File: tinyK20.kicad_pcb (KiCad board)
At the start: 2 copper layers, 46 x 74.4 mm, 79 parts, among them CON1 USB-MINI-B, P1 CONN_1, P10 CONN_1, P11 CONN_1, P12 CONN_1, P13 CONN_1, P14 CONN_1, P15 CONN_1, P16 CONN_1, P17 CONN_1, P18 CONN_1, P19 CONN_1, P2 CONN_1, P20 CONN_1, P21 CONN_1, P22 CONN_1, P23 CONN_1, P24 CONN_1, P25 CONN_1, P26 CONN_1, P27 CONN_1, P28 CONN_1, P29 CONN_1, P3 CONN_1, P30 CONN_1, P31 CONN_1, P33 CONN_1, P34 CONN_1, P35 CONN_5X2, P37 CONN_1, P38 CONN_5X2, P4 CONN_1, P41 CONN_1, P5 CONN_1, P6 CONN_1, P7 CONN_1, P8 CONN_1, P9 CONN_1, SW1 SW_PUSH, U1 MK20DX128VFT5, U2 LT1129CST-3.3, U3 74LS126, U4 105027-0001, Y1 Crystal, Y2 Crystal_Small

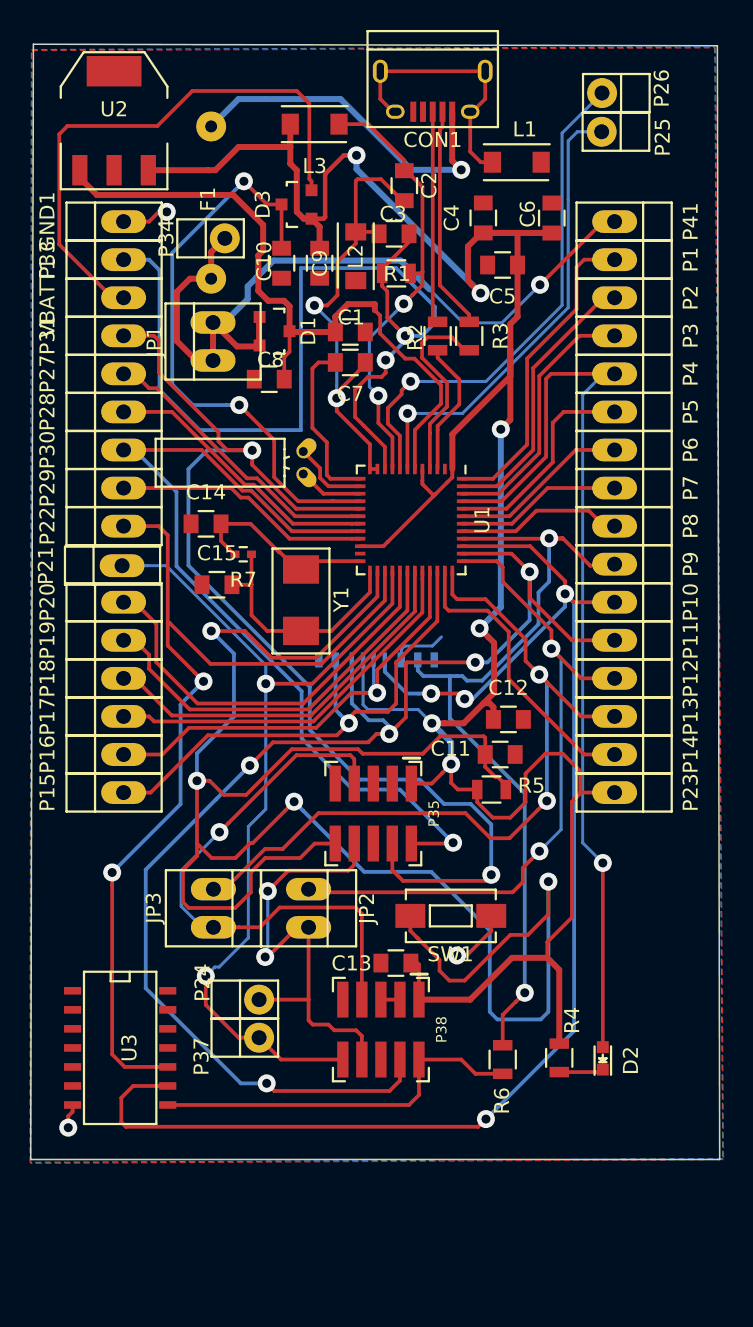
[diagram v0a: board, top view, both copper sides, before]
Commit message: Get rid of ground plane on top copper.
 Add optional vias. Re-route tracks
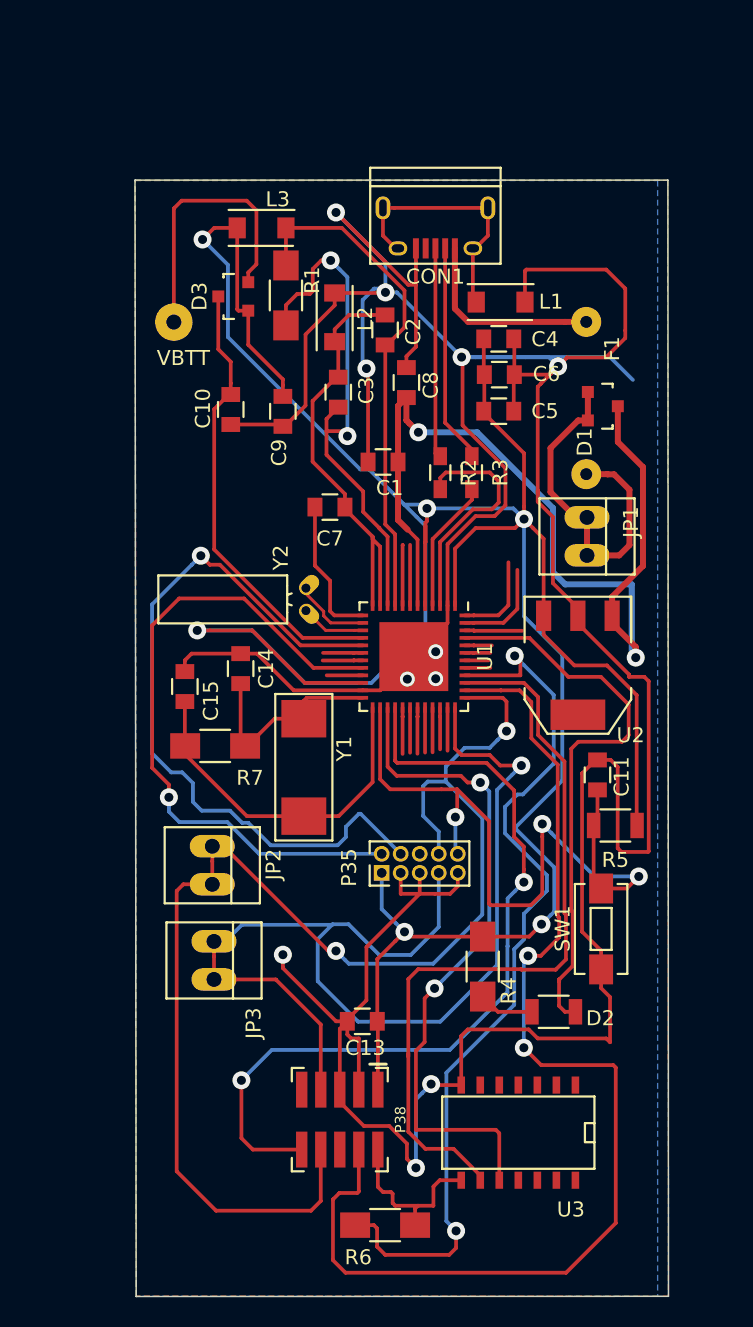
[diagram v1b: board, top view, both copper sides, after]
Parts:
- removed C12: 2.2u, Capacitors_SMD:C_0805
- removed GND1, P1, P10, P11, P12, P13, P14, P15, P16, P17, P18, P19, P2, P20, P21, P22, P23, P27, P28, P29, P3, P30, P31, P33, P4, P41, P5, P6, P7, P8, P9, VBATT1: CONN_1, Connect:PIN1
- removed P24, P25, P26, P34, P37: CONN_1, Connect:PINC
- removed U4: 105027-0001, sd-socket:105027-0001
- added VBTT: CONN_1, Wire_Pads:SolderWirePad_single_1mmDrill, F.Cu at (58.8, 38.8)
- D2: footprint LEDs:LED_0603 -> Resistors_SMD:R_1206
- P35: footprint Connect:CONN-2x5-1.27-SMT -> Pin_Headers:Pin_Header_Straight_2x05_Pitch1.27mm
- R1, R4, R6: footprint Resistors_SMD:R_0805 -> Resistors_SMD:R_1206_HandSoldering
- R2, R3: footprint Resistors_SMD:R_0805 -> Resistors_SMD:R_0603_HandSoldering
- R5: footprint Resistors_SMD:R_0805 -> Resistors_SMD:R_1206
- R7: footprint Capacitors_SMD:C_0402 -> Resistors_SMD:R_1206_HandSoldering
- Y1: footprint Crystals:ABM3 -> Housings_DFN_QFN:ABM3
- moved U2 47.7 mm to (85.7, 61.7), turned to 180 degrees
- moved F1 28.2 mm to (86.3, 38.8)
- moved JP1 28.1 mm to (86.3, 53.1), turned to 270 degrees
- moved U3 27.1 mm to (81.8, 93.0), turned to 180 degrees
- moved D1 22.5 mm to (87.4, 44.4)
- moved R6 13.6 mm to (72.9, 99.1), turned to 0 degrees
- moved R7 12.9 mm to (61.5, 67.1), turned to 0 degrees
- moved C3 11.2 mm to (69.7, 43.5), turned to 90 degrees
- moved C6 11.0 mm to (80.5, 42.3), turned to 0 degrees
- moved C10 10.3 mm to (62.6, 44.6)
- moved C9 10.2 mm to (66.1, 44.8)
- moved SW1 10.1 mm to (87.3, 79.3), turned to 90 degrees
- moved Y1 9.96 mm to (67.4, 65.3)
- moved C14 9.93 mm to (63.2, 61.9), turned to 270 degrees
- moved C5 9.76 mm to (80.5, 44.8), turned to 0 degrees
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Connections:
- JP2 pad 1: Net-(JP2-Pad1) -> UART1_TX
- JP3 pad 1: Net-(JP3-Pad1) -> UART1_RX
- U1 pad 18: Net-(P27-Pad1) -> (no net)
- U1 pad 19: Net-(P28-Pad1) -> (no net)
- U1 pad 21: Net-(P29-Pad1) -> (no net)
- U1 pad 29: Net-(P20-Pad1) -> (no net)
- U1 pad 30: Net-(P19-Pad1) -> (no net)
- U1 pad 31: Net-(P18-Pad1) -> (no net)
- U1 pad 32: Net-(P17-Pad1) -> (no net)
- U1 pad 33: PTC0 -> (no net)
- U1 pad 34: PTC1 -> (no net)
- U1 pad 35: Net-(P14-Pad1) -> (no net)
- U1 pad 36: Net-(JP3-Pad1) -> UART1_RX
- U1 pad 37: Net-(JP2-Pad1) -> UART1_TX
- U1 pad 41: Net-(P8-Pad1) -> (no net)
- U1 pad 42: Net-(P7-Pad1) -> (no net)
- U1 pad 43: Net-(P6-Pad1) -> (no net)
- U1 pad 44: Net-(P5-Pad1) -> (no net)
- U1 pad 46: Net-(P3-Pad1) -> (no net)
- U1 pad 47: Net-(P2-Pad1) -> (no net)
- U1 pad 48: Net-(P1-Pad1) -> (no net)
- U1 pad 7: Net-(P25-Pad1) -> (no net)
- U1 pad 8: Net-(P26-Pad1) -> (no net)
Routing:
- net GND: track 14.7 -> 283.0 mm, vias 3 -> 11
- net RESET: track 133.4 -> 50.2 mm, vias 4 -> 3
- net (no net): track 0.00 -> 59.9 mm
- net UART1_TX: track 34.1 -> 88.2 mm
- net Net-(JP3-Pad1): track 51.3 -> 0.00 mm, vias 2 -> 0
- net Net-(JP2-Pad1): track 47.0 -> 0.00 mm, vias 2 -> 0
- net PTC6: track 97.4 -> 51.4 mm, vias 4 -> 0
- net UART1_RX: track 38.0 -> 76.4 mm
- net PTC1: track 35.4 -> 0.00 mm, vias 1 -> 0
- net Net-(P26-Pad1): track 34.3 -> 0.00 mm, vias 1 -> 0
- net Net-(P25-Pad1): track 31.0 -> 0.00 mm, vias 1 -> 0
- net Net-(D1-Pad1): track 54.7 -> 24.1 mm, vias 1 -> 0
- net PTC0: track 30.5 -> 0.00 mm, vias 1 -> 0
- net Net-(C3-Pad1): track 65.3 -> 35.4 mm
- net Net-(P20-Pad1): track 27.8 -> 0.00 mm
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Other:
- board size 46 x 74.4 mm -> 35.6 x 74.5 mm
- rule trace_min: 0.1 -> 0.006
- rule via_min_drill: 0.6 -> 0.013
- rule via_min_size: 1.2 -> 0.027
